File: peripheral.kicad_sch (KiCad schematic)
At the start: 30 parts, among them J10 SONAR, J11 NRF, J5 Micro_SD_Card, J6 micro_sd, J7 SSD1306_128x32_OLED, J8 HC-SR04, J9 NRF_24_socket, U1 LIS3DH, U2 APDS-9306-065, U4 M24256-BR (MB85RC16V), U6 SN74LVC1G14DBV, U8 MT3608, U9 SHT30-DIS

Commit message: fit test
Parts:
- added C53, C55, C57: 100n 50V, Capacitor_SMD:C_0603_1608Metric, symbol Device:C_Small
- added C54, C56: 10u 10V, Capacitor_SMD:C_0603_1608Metric, symbol Device:C_Small
- added J6: OLED I2C, Connector_PinHeader_2.54mm:PinHeader_1x02_P2.54mm_Vertical, symbol Connector_Generic:Conn_01x02
- added J7: VL53_PINS, Connector_PinHeader_2.54mm:PinHeader_1x02_P2.54mm_Vertical, symbol Connector_Generic:Conn_01x02
- added J9: I2C, Connector_PinHeader_2.54mm:PinHeader_1x02_P2.54mm_Vertical, symbol Connector_Generic:Conn_01x02
- added JP5: NO, Jumper:SolderJumper-2_P1.3mm_Open_RoundedPad1.0x1.5mm, symbol Jumper:Jumper_2_Small_Open
- added R21, R22, R25, R26: 2k2 1%, Resistor_SMD:R_0603_1608Metric_Pad0.98x0.95mm_HandSolder, symbol Device:R_Small
- added R23, R24: 10k 1%, Resistor_SMD:R_0603_1608Metric_Pad0.98x0.95mm_HandSolder, symbol Device:R_Small
- added U9: VL53L0CXV0DH1, Sensor_Distance:ST_VL53L1x, symbol Sensor_Distance:VL53L0CXV0DH1
- U1: jlc (none) -> C15134
- U10: renamed from U9; jlc (none) -> C2687423
- U4: value M24256-BR (MB85RC16V) -> M24256-BR; M Fujitsu -> STMicroelectronics; MPN MB85RC16PNF-G-JNERE1 -> M24256-BRMN6TP; jlc (none) -> C79984
- renumbered J10 to J19, J6 to J20, J9 to J21, J7 to J22
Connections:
- net +3V3: now also U1.1 (VDD_IO), U1.14 (VDD), U1.8 (CS), U10.5 (VDD), C53.1, C54.1, C55.1, C56.1, C57.1, R21.1, R22.1, R23.2, R24.2, R25.1, R26.1, U9.1 (AVDDVCSEL), U9.11 (AVDD)
- net GND: now also U1.10 (GND), U1.12 (GND), U1.13 (ADC3), U1.15 (ADC2), U1.16 (ADC1), U1.5 (GND), U10.2 (ADDR), U10.7 (R), U10.8 (VSS), U10.9 (VSS), C53.2, C54.2, C55.2, C56.2, C57.2, JP5.1 (A), U9.12 (GND), U9.2 (AVSSVCSEL), U9.3 (GND), U9.4 (GND), U9.6 (GND)
- net OLED_SCL: now also J6.2 (Pin_2), R22.2
- net OLED_SDA: now also J6.1 (Pin_1), R21.2
- net SCL: now also U1.4 (SPC), U10.4 (SCL), J9.1 (Pin_1), R25.2, U9.10 (SCL)
- net SDA: now also U1.6 (SDI), U10.1 (SDA), J9.2 (Pin_2), R26.2, U9.9 (SDA)
- net at U1.7 (SDO): now also JP5.2 (B)
- net GPIO18: no longer names the net of J20.3 (Pin_3), J5.3 (CMD)
- net GPIO19: no longer names the net of J20.5 (Pin_5), J5.7 (DAT0)
- net GPIO22: no longer names the net of J20.2 (Pin_2), J5.2 (DAT3/CD)
- net GPIO5: no longer names the net of J20.4 (Pin_4), J5.5 (CLK), R13.1
- net SD_DAT1: no longer names the net of J20.6 (Pin_6), J5.8 (DAT1), R9.1
- net SD_DAT2: no longer names the net of J20.1 (Pin_1), J5.1 (DAT2), R11.1
- new net: J7.2 (Pin_2), R23.1, U9.5 (XSHUT)
- new net: J7.1 (Pin_1), R24.1, U9.7 (GPIO1)
- no-connect marks 4 -> 8
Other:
- note added: "OLED gets a separate I2C interface"
- moved on the sheet: C1, C3, C31, J22, U1, U10, U2, U4

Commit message: layout
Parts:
- L1: footprint Inductor_SMD:L_Wuerth_MAPI-3020 -> Inductor_SMD:L_1206_3216Metric_Pad1.22x1.90mm_HandSolder; M TDK -> FH (Guangdong Fenghua Advanced Tech); MPN VLS3015ET-4R7M -> CMP321609UD4R7MT; jlc (none) -> C139250
- R17: footprint Resistor_SMD:R_0603_1608Metric -> Resistor_SMD:R_0603_1608Metric_Pad0.98x0.95mm_HandSolder
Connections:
- net +3V3: now also J21.1 (Pin_1); no longer J21.2 (Pin_2)
- net GND: now also J21.2 (Pin_2); no longer J21.1 (Pin_1)
- net NRF_CE: now also J21.4 (Pin_4); no longer J21.3 (Pin_3)
- net NRF_CNS: now also J21.3 (Pin_3); no longer J21.4 (Pin_4)
- net NRF_IRQ: now also J21.7 (Pin_7); no longer J21.8 (Pin_8)
- net NRF_MISO: now also J21.8 (Pin_8); no longer J21.7 (Pin_7)
- net NRF_MOSI: now also J21.5 (Pin_5); no longer J21.6 (Pin_6)
- net NRF_SCK: now also J21.6 (Pin_6); no longer J21.5 (Pin_5)
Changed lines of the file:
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@@
 	(wire
 		(pts
-			(xy 184.15 99.06) (xy 184.15 100.33)
+			(xy 34.29 119.38) (xy 31.75 119.38)
 		)
 		(stroke
@@
 	(wire
 		(pts
-			(xy 44.45 58.42) (xy 86.36 58.42)
+			(xy 184.15 99.06) (xy 184.15 100.33)
 		)
 		(stroke
@@
 	(wire
 		(pts
-			(xy 264.16 30.48) (xy 264.16 33.02)
+			(xy 44.45 58.42) (xy 86.36 58.42)
 		)
 		(stroke
@@
 	(wire
 		(pts
-			(xy 246.38 25.4) (xy 248.92 25.4)
+			(xy 264.16 30.48) (xy 264.16 33.02)
 		)
 		(stroke
@@
 	(wire
 		(pts
-			(xy 31.75 111.76) (xy 34.29 111.76)
+			(xy 246.38 25.4) (xy 248.92 25.4)
 		)
 		(stroke
@@
 	(wire
 		(pts
-			(xy 31.75 119.38) (xy 34.29 119.38)
-		)
-		(stroke
-			(width 0)
-			(type default)
-		)
-	)
-	(wire
-		(pts
 			(xy 184.15 31.75) (xy 190.5 31.75)
 		)
@@
 	(wire
 		(pts
+			(xy 34.29 111.76) (xy 31.75 111.76)
+		)
+		(stroke
+			(width 0)
+			(type default)
+		)
+	)
+	(wire
+		(pts
 			(xy 246.38 30.48) (xy 264.16 30.48)
 		)
@@
 	(symbol
 		(lib_id "Connector_Generic:Conn_02x04_Odd_Even")
-		(at 39.37 114.3 0)
+		(at 41.91 114.3 0)
+		(mirror y)
 		(unit 1)
 		(exclude_from_sim no)
@@
 		(dnp no)
 		(property "Reference" "J21"
-			(at 40.386 108.966 0)
+			(at 40.894 108.966 0)
 			(effects
 				(font
@@
 		)
 		(property "Value" "NRF_24_socket"
-			(at 41.148 122.428 0)
+			(at 40.132 122.428 0)
 			(effects
 				(font
@@
 		)
 		(property "Footprint" "Connector_PinSocket_2.54mm:PinSocket_2x04_P2.54mm_Vertical"
-			(at 39.37 114.3 0)
+			(at 41.91 114.3 0)
 			(effects
 				(font
@@
 		)
 		(property "Datasheet" "~"
-			(at 39.37 114.3 0)
+			(at 41.91 114.3 0)
 			(effects
 				(font
@@
 		)
 		(property "Description" "Generic connector, double row, 02x04, odd/even pin numbering scheme (row 1 odd numbers, row 2 even numbers), script generated (kicad-library-utils/schlib/autogen/connector/)"
-			(at 39.37 114.3 0)
+			(at 41.91 114.3 0)
 			(effects
 				(font
@@
 			)
 		)
-		(property "Footprint" "Inductor_SMD:L_Wuerth_MAPI-3020"
+		(property "Footprint" "Inductor_SMD:L_1206_3216Metric_Pad1.22x1.90mm_HandSolder"
 			(at 124.46 160.02 0)
 			(effects
@@
 			)
 		)
-		(property "Datasheet" "https://product.tdk.com/system/files/dam/doc/product/inductor/inductor/smd/catalog/inductor_commercial_power_vls3012hbx_en.pdf"
+		(property "Datasheet" ""
 			(at 124.46 160.02 0)
 			(effects
@@
 			)
 		)
-		(property "M" "TDK"
+		(property "M" "FH (Guangdong Fenghua Advanced Tech)"
+			(at 124.46 160.02 90)
+			(effects
+				(font
+					(size 1.27 1.27)
+				)
+				(hide yes)
+			)
+		)
+		(property "MPN" "CMP321609UD4R7MT"
 			(at 124.46 160.02 90)
 			(effects
@@
 			)
 		)
-		(property "MPN" "VLS3015ET-4R7M"
+		(property "jlc" "C139250"
 			(at 124.46 160.02 90)
 			(effects
@@
 			)
 		)
-		(property "Footprint" "Resistor_SMD:R_0603_1608Metric"
+		(property "Footprint" "Resistor_SMD:R_0603_1608Metric_Pad0.98x0.95mm_HandSolder"
 			(at 68.58 186.69 0)
 			(effects

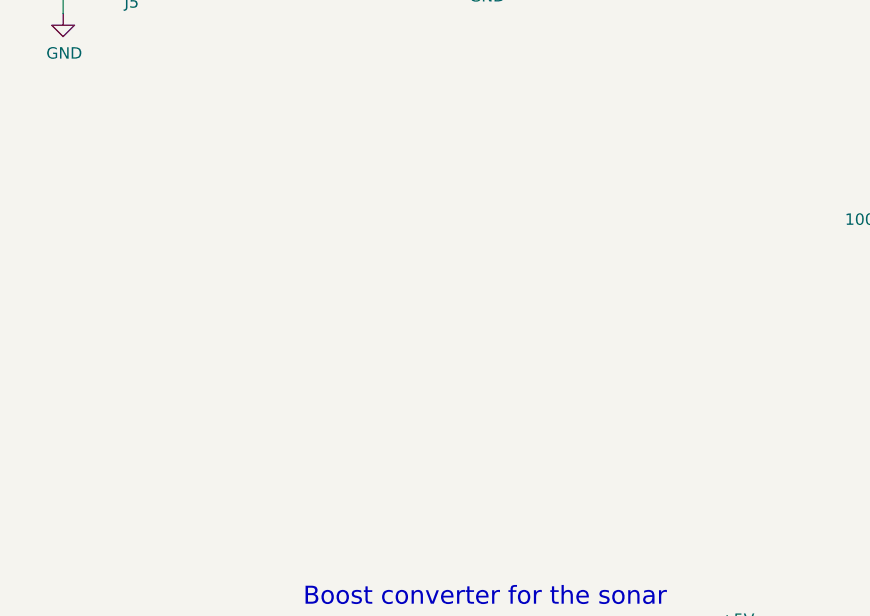
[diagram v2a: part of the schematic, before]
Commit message: preparing for more modules
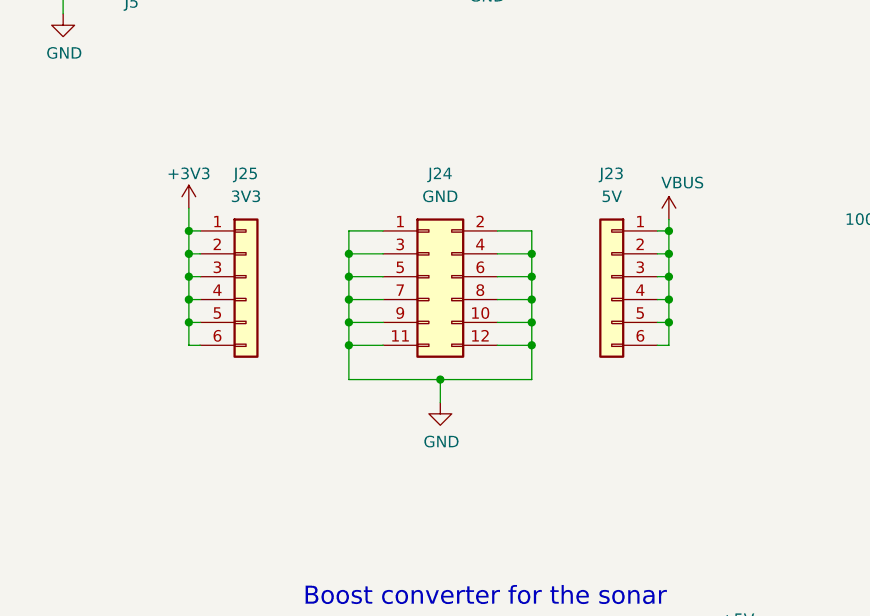
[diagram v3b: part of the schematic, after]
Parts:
- added J23: 5V, Connector_PinHeader_2.54mm:PinHeader_1x06_P2.54mm_Vertical, symbol Connector_Generic:Conn_01x06
- added J24: GND, symbol Connector_Generic:Conn_02x06_Odd_Even
- added J25: 3V3, Connector_PinHeader_2.54mm:PinHeader_1x06_P2.54mm_Vertical, symbol Connector_Generic:Conn_01x06
- J11, J20: jlc C585350 -> C37208
- J5: jlc (none) -> C585350
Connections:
- net +3V3: now also J25.1 (Pin_1), J25.2 (Pin_2), J25.3 (Pin_3), J25.4 (Pin_4), J25.5 (Pin_5), J25.6 (Pin_6)
- net GND: now also J24.1 (Pin_1), J24.10 (Pin_10), J24.11 (Pin_11), J24.12 (Pin_12), J24.2 (Pin_2), J24.3 (Pin_3), J24.4 (Pin_4), J24.5 (Pin_5), J24.6 (Pin_6), J24.7 (Pin_7), J24.8 (Pin_8), J24.9 (Pin_9)
- new net VBUS: J23.1 (Pin_1), J23.2 (Pin_2), J23.3 (Pin_3), J23.4 (Pin_4), J23.5 (Pin_5), J23.6 (Pin_6)

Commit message: more stuff added to sch
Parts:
- removed J23: 5V, Connector_PinHeader_2.54mm:PinHeader_1x06_P2.54mm_Vertical, symbol Connector_Generic:Conn_01x06
- removed J24: GND, symbol Connector_Generic:Conn_02x06_Odd_Even
- removed J25: 3V3, Connector_PinHeader_2.54mm:PinHeader_1x06_P2.54mm_Vertical, symbol Connector_Generic:Conn_01x06
- added R36: 10k 1%, Resistor_SMD:R_0603_1608Metric_Pad0.98x0.95mm_HandSolder, symbol Device:R_Small
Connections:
- net +3V3: now also R36.1
- net SONAR_TRIG: now also R36.2

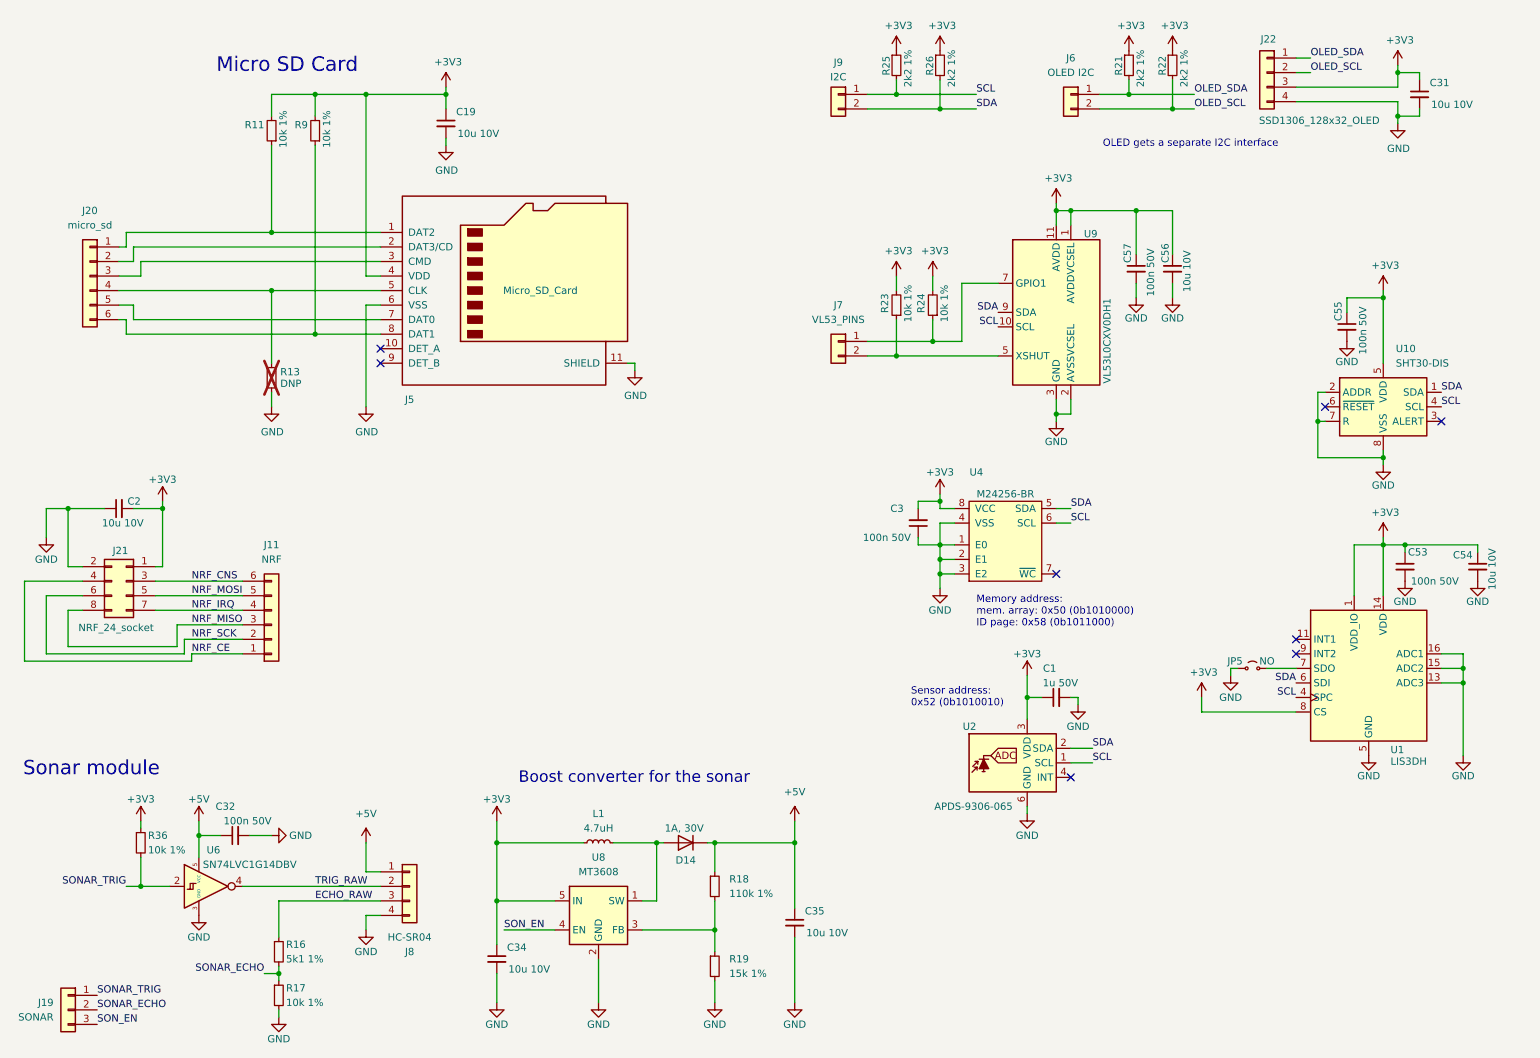
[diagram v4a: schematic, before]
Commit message: kju fix and PCB size increase
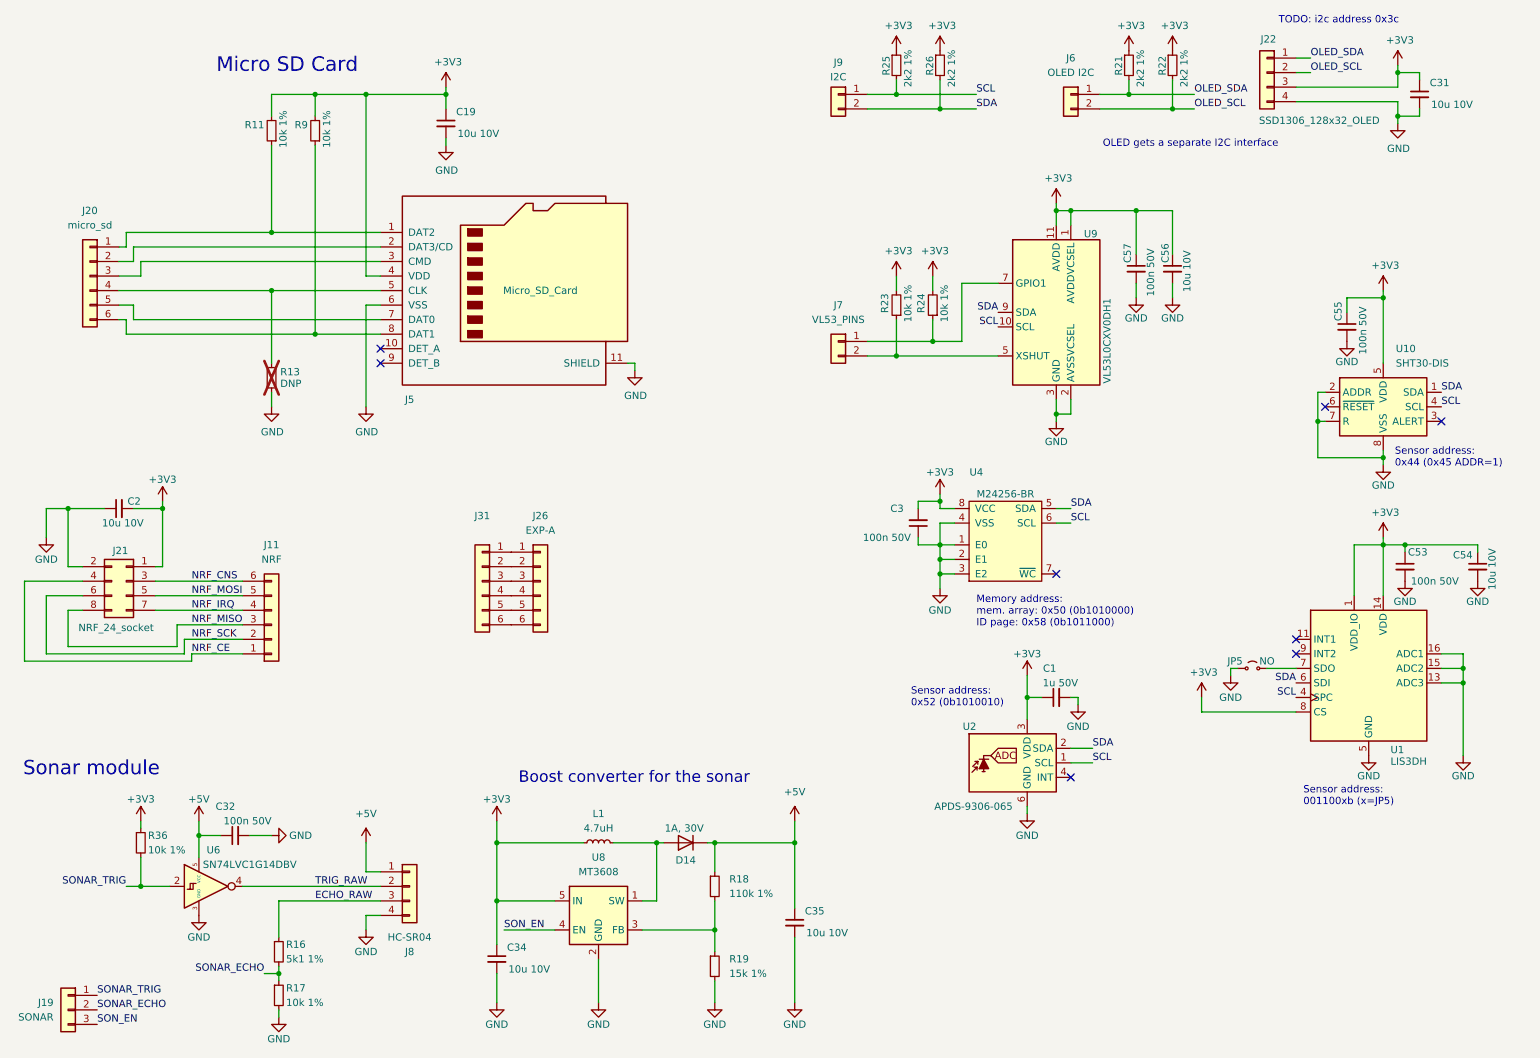
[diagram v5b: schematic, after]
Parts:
- added J26: EXP-A, Connector_PinHeader_2.54mm:PinHeader_1x06_P2.54mm_Vertical, symbol Connector_Generic:Conn_01x06
- added J31: ~, Connector_PinSocket_2.54mm:PinSocket_1x06_P2.54mm_Vertical, symbol Connector_Generic:Conn_01x06
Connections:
- new net: J26.1 (Pin_1), J31.1 (Pin_1)
- new net: J26.2 (Pin_2), J31.2 (Pin_2)
- new net: J26.3 (Pin_3), J31.3 (Pin_3)
- new net: J26.4 (Pin_4), J31.4 (Pin_4)
- new net: J26.5 (Pin_5), J31.5 (Pin_5)
- new net: J26.6 (Pin_6), J31.6 (Pin_6)
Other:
- note added: "Sensor address: 001100xb (x=JP5)"
- note added: "Sensor address: 0x44 (0x45 ADDR=1)"
- note added: "TODO: i2c address 0x3c"
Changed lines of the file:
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@@
 		)
 	)
+	(text "TODO: i2c address 0x3c"
+		(exclude_from_sim no)
+		(at 243.332 17.018 0)
+		(effects
+			(font
+				(size 1.27 1.27)
+			)
+			(justify left bottom)
+		)
+	)
+	(text "Sensor address: \n0x44 (0x45 ADDR=1)\n\n"
+		(exclude_from_sim no)
+		(at 263.652 96.52 0)
+		(effects
+			(font
+				(size 1.27 1.27)
+			)
+			(justify left bottom)
+		)
+	)
 	(text "Sonar module"
 		(exclude_from_sim no)
@@
 		)
 	)
+	(text "Sensor address: \n001100xb (x=JP5)\n\n"
+		(exclude_from_sim no)
+		(at 247.65 155.702 0)
+		(effects
+			(font
+				(size 1.27 1.27)
+			)
+			(justify left bottom)
+		)
+	)
 	(text "OLED gets a separate I2C interface"
 		(exclude_from_sim no)
@@
 	)
 	(symbol
+		(lib_id "Connector_Generic:Conn_01x06")
+		(at 104.14 114.3 0)
+		(mirror y)
+		(unit 1)
+		(exclude_from_sim no)
+		(in_bom yes)
+		(on_board yes)
+		(dnp no)
+		(property "Reference" "J31"
+			(at 104.14 102.87 0)
+			(effects
+				(font
+					(size 1.27 1.27)
+				)
+			)
+		)
+		(property "Value" "~"
+			(at 104.14 105.41 0)
+			(effects
+				(font
+					(size 1.27 1.27)
+				)
+			)
+		)
+		(property "Footprint" "Connector_PinSocket_2.54mm:PinSocket_1x06_P2.54mm_Vertical"
+			(at 104.14 114.3 0)
+			(effects
+				(font
+					(size 1.27 1.27)
+				)
+				(hide yes)
+			)
+		)
+		(property "Datasheet" "~"
+			(at 104.14 114.3 0)
+			(effects
+				(font
+					(size 1.27 1.27)
+				)
+				(hide yes)
+			)
+		)
+		(property "Description" "Generic connector, single row, 01x06, script generated (kicad-library-utils/schlib/autogen/connector/)"
+			(at 104.14 114.3 0)
+			(effects
+				(font
+					(size 1.27 1.27)
+				)
+				(hide yes)
+			)
+		)
+		(property "jlc" "C37208"
+			(at 104.14 114.3 0)
+			(effects
+				(font
+					(size 1.27 1.27)
+				)
+				(hide yes)
+			)
+		)
+		(pin "4"
+		)
+		(pin "1"
+		)
+		(pin "6"
+		)
+		(pin "3"
+		)
+		(pin "5"
+		)
+		(pin "2"
+		)
+		(instances
+			(project "beam_kit_1"
+				(path "/3a707576-1044-44db-8cf8-deb84fe605c8/896b7e04-9267-4f9a-9246-5bddfae4281c"
+					(reference "J31")
+					(unit 1)
+				)
+			)
+		)
+	)
+	(symbol
 		(lib_id "Device:C_Small")
 		(at 204.47 134.62 90)
@@
 					(unit 1)
 				)
+			)
+		)
+	)
+	(symbol
+		(lib_id "Connector_Generic:Conn_01x06")
+		(at 114.3 114.3 0)
+		(unit 1)
+		(exclude_from_sim no)
+		(in_bom yes)
+		(on_board yes)
+		(dnp no)
+		(property "Reference" "J26"
+			(at 114.3 102.87 0)
+			(effects
+				(font
+					(size 1.27 1.27)
+				)
+			)
+		)
+		(property "Value" "EXP-A"
+			(at 114.3 105.41 0)
+			(effects
+				(font
+					(size 1.27 1.27)
+				)
+			)
+		)
+		(property "Footprint" "Connector_PinHeader_2.54mm:PinHeader_1x06_P2.54mm_Vertical"
+			(at 114.3 114.3 0)
+			(effects
+				(font
+					(size 1.27 1.27)
+				)
+				(hide yes)
+			)
+		)
+		(property "Datasheet" "~"
+			(at 114.3 114.3 0)
+			(effects
+				(font
+					(size 1.27 1.27)
+				)
+				(hide yes)
+			)
+		)
+		(property "Description" "Generic connector, single row, 01x06, script generated (kicad-library-utils/schlib/autogen/connector/)"
+			(at 114.3 114.3 0)
+			(effects
+				(font
+					(size 1.27 1.27)
+				)
+				(hide yes)
+			)
+		)
+		(property "jlc" "C37208"
+			(at 114.3 114.3 0)
+			(effects
+				(font
+					(size 1.27 1.27)
+				)
+				(hide yes)
+			)
+		)
+		(pin "4"
+		)
+		(pin "1"
+		)
+		(pin "6"
+		)
+		(pin "3"
+		)
+		(pin "5"
+		)
+		(pin "2"
+		)
+		(instances
+			(project "beam_kit_1"
+				(path "/3a707576-1044-44db-8cf8-deb84fe605c8/896b7e04-9267-4f9a-9246-5bddfae4281c"
+					(reference "J26")
+					(unit 1)
+				)
